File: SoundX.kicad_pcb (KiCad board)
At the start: 2 copper layers, 60.8 x 99.9 mm, 51 parts, among them CN1 EDGE_CONN, CN2 AUDIO_OUT, CN3 CONN_MIDI_IN, CN4 CONN_MIDI_OUT, U1 GAL20V8, U2 MC6850, U3 YM3526, U4 6N138, U6 YM3014, U7 LM324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

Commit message: Add clock divider for ACIA
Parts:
- added C12: 100n, Capacitor_THT:C_Disc_D7.0mm_W2.5mm_P5.00mm, F.Cu at (170.3, 90.8)
- added JP7: JMP_ACIA_CLK, Jumper:SolderJumper-3_P1.3mm_Open_RoundedPad1.0x1.5mm, B.Cu at (167.6, 98.3)
- added U5: 74HCT74, Package_DIP:DIP-14_W7.62mm_Socket_LongPads, F.Cu at (164.0, 94.6)
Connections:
- FB3 pad 1: /clock_acia -> /clk
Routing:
- net /clk: track 0.00 -> 60.3 mm, vias 0 -> 1
- net +5V: track 243.3 -> 298.8 mm, vias 4 -> 5
- net /clock_acia: track 60.6 -> 12.3 mm, vias 1 -> 0
- net /clk_quarter: track 0.00 -> 16.0 mm, vias 0 -> 2
- net Net-(U5A-D): track 0.00 -> 14.0 mm
- net Net-(U5B-D): track 0.00 -> 11.5 mm
- net /rxd_ttl: track 30.1 -> 41.0 mm, vias 1 -> 2
- net /d0: track 103.9 -> 114.4 mm, vias 3 -> 2
- net /clk_half: track 0.00 -> 10.2 mm, vias 0 -> 2
- net /ext_audio: track 138.2 -> 148.4 mm
- net /d1: track 101.4 -> 108.1 mm, vias 4 -> 2
- net /d6: track 71.4 -> 65.2 mm
- net /d7: track 76.1 -> 70.1 mm
- net /r_~{w}: track 124.6 -> 128.6 mm, vias 4 -> 3
- net /clock_ym: track 30.9 -> 32.0 mm
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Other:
- board text added: "(Set JP7 accordingly!)"
- board text added: "2M"
- board text added: "500 KHz or 2 MHz"
- board text added: "500k"
- board text added: "CC-BY-NC-SA © SukkoPera/Kinmami 2023-2024 github.com/SukkoPera/SoundX"
- board text added: "GAL20V8 or GAL22V10"
- board text removed: "500 KHz"
- board text removed: "CC-BY-NC-SA © SukkoPera/Kinmami 2023 github.com/SukkoPera/SoundX"
- board text removed: "GAL20V8 or GAL22V16"

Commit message: Final touches
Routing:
- net /d6: track 65.2 -> 64.1 mm, vias 2 -> 1
- net /d2: track 68.0 -> 69.1 mm
- net /clk_quarter: track 16.0 -> 16.9 mm
- net /d5: track 64.6 -> 64.2 mm, vias 1 -> 2
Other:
- board text added: "500 kHz or 2 MHz"
- board text removed: "500 KHz or 2 MHz"

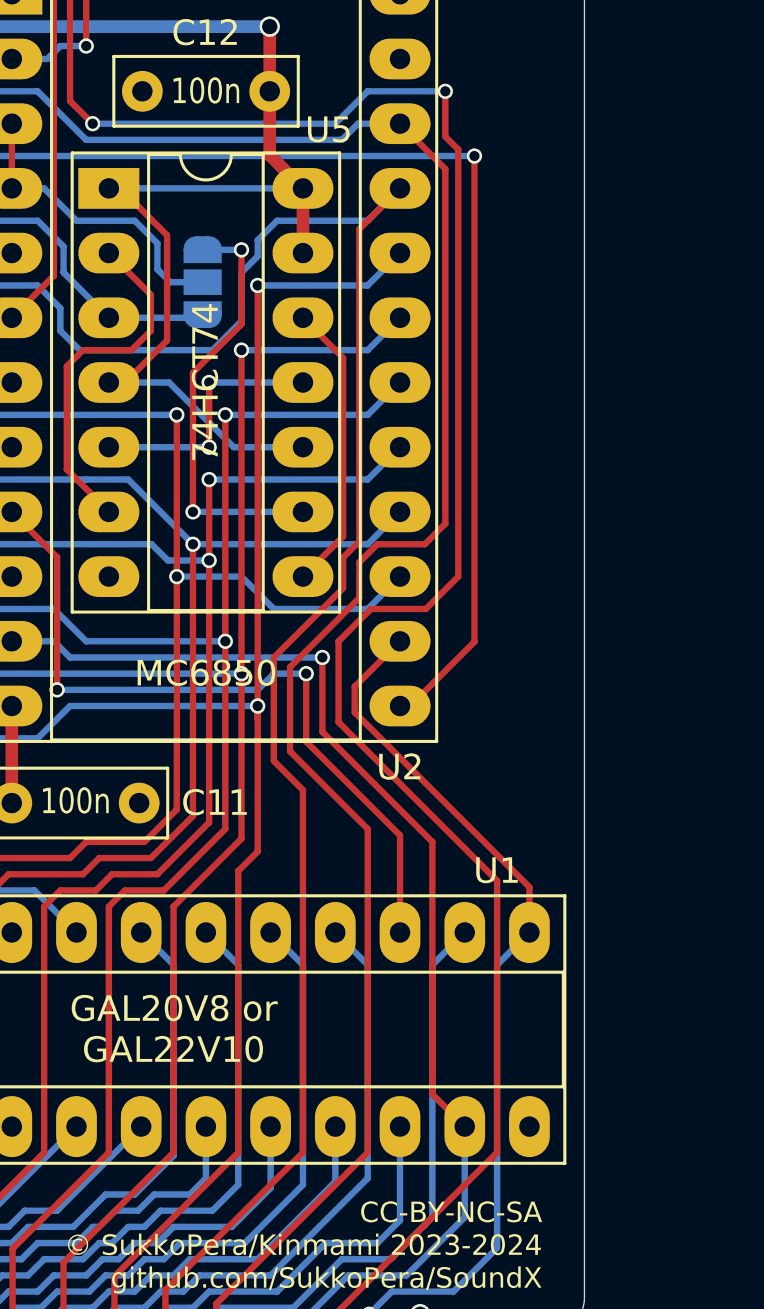
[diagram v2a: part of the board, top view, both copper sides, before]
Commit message: Add RW/A1 jumper This is inspired by some C64 interfaces
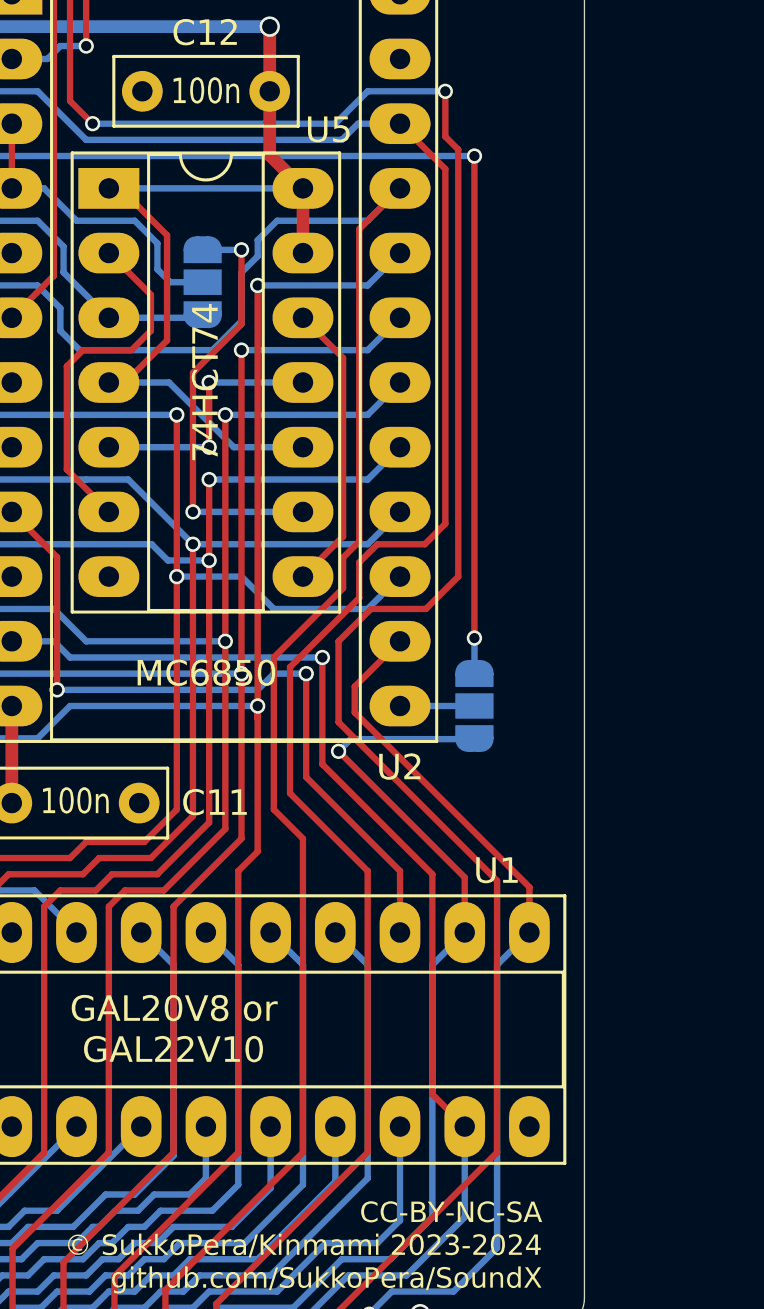
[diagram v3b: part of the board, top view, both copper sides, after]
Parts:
- added JP8: JMP_RW, Jumper:SolderJumper-3_P1.3mm_Open_RoundedPad1.0x1.5mm, B.Cu at (178.3, 114.9)
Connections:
- U2 pad 13: /r_~{w} -> Net-(JP8-C)
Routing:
- net /a1: track 28.6 -> 43.3 mm, vias 0 -> 1
- net Net-(JP8-C): track 0.00 -> 2.92 mm
- net /r_~{w}: track 128.6 -> 126.2 mm, vias 3 -> 4

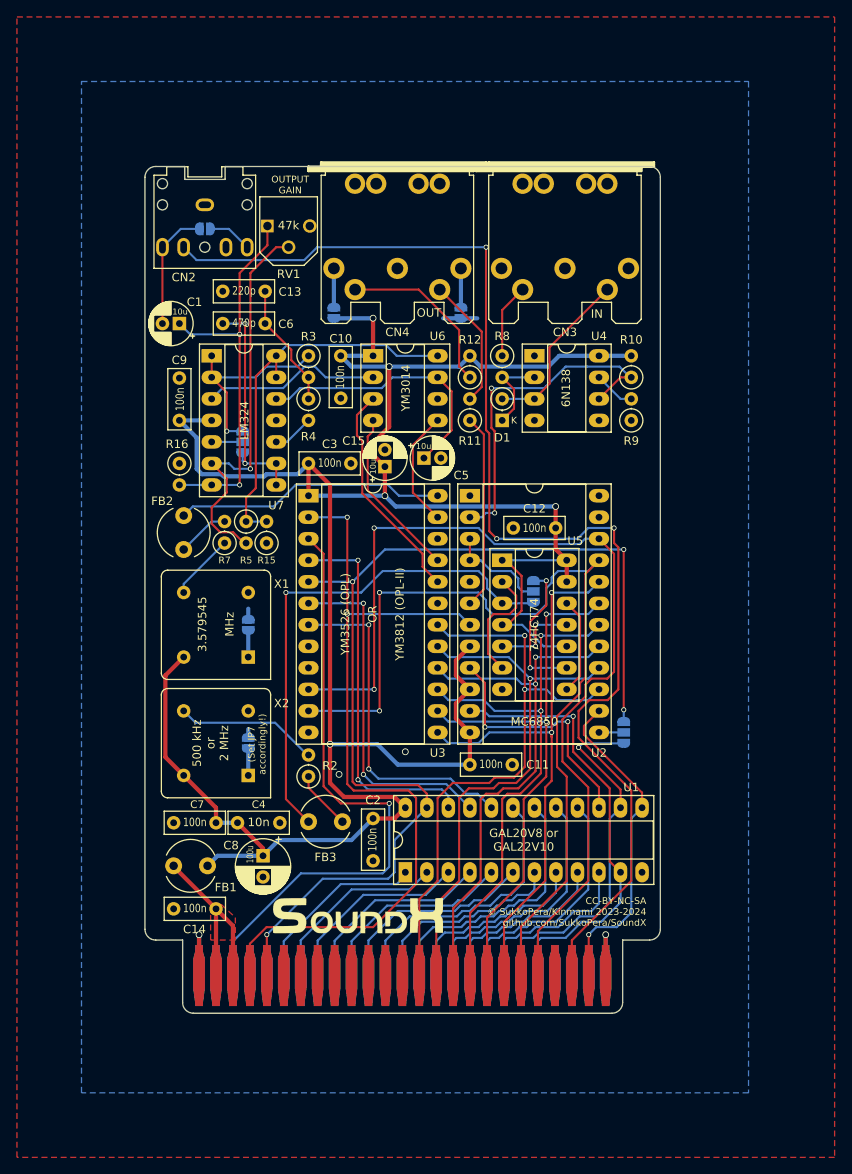
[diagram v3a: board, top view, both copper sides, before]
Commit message: 44-pin version of V2
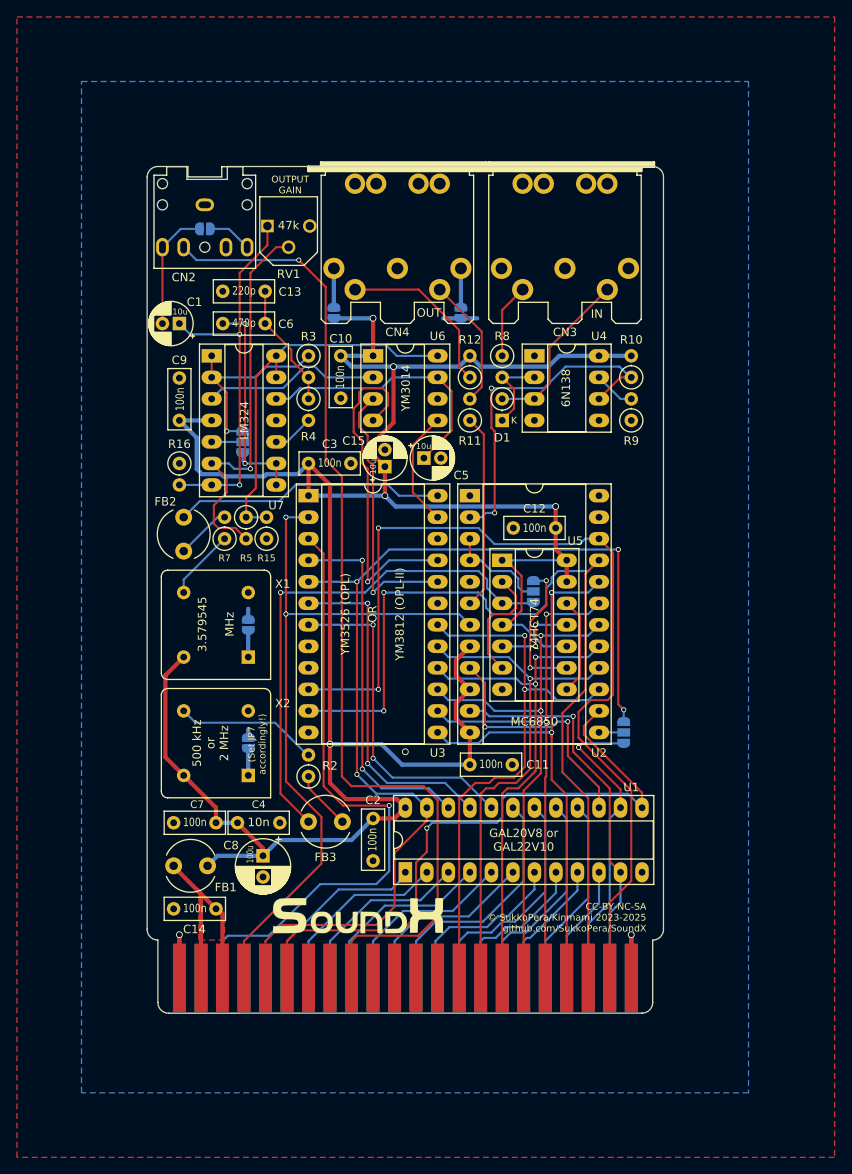
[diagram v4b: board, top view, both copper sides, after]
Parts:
- CN1: footprint SoundX:C16_Cart_Conn -> SoundX:EdgeConn-44pin
- moved CN1 29.2 mm to (123.3, 147.8)
- moved R5 0.51 mm to (133.7, 89.5)
- moved R15 0.51 mm to (136.1, 92.1)
- moved R7 0.51 mm to (131.2, 92.1)
- moved FB2 0.19 mm to (126.4, 89.5)
- turned JP8 to 90 degrees
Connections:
- CN1 pad 22: unconnected-(CN1-AEC-Pad22) -> GND
- CN1 pad 6: unconnected-(CN1-C1HI-Pad6) -> /phi2
- CN1 pad 9: unconnected-(CN1-/CS1-Pad9) -> /ext_audio
- CN1 pad Z: unconnected-(CN1-NC-PadZ) -> GND
- JP8 pad 1: /r_~{w} -> /a1
- JP8 pad 3: /a1 -> /r_~{w}
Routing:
- net /phi2: track 39.3 -> 75.7 mm
- net /ext_audio: track 148.4 -> 119.2 mm, vias 3 -> 1
- net /ser_audio: track 20.2 -> 40.4 mm, vias 0 -> 1
- net /~{irq}: track 96.7 -> 84.8 mm
- net /a2: track 21.2 -> 13.8 mm
- net /a1: track 43.3 -> 36.1 mm
- net /a0: track 52.8 -> 45.9 mm
- net /a4: track 21.7 -> 15.0 mm
- net /a3: track 29.1 -> 22.4 mm
- net /a5: track 30.7 -> 24.5 mm
- net /dac_clk: track 26.3 -> 32.4 mm, vias 0 -> 1
- net /a6: track 23.4 -> 17.7 mm
- net /a7: track 32.2 -> 27.1 mm
- net /a9: track 33.0 -> 28.9 mm
- net /a8: track 24.6 -> 20.6 mm
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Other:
- board size 60.8 x 99.9 mm -> 61 x 99.9 mm
- board text added: "A1"
- board text added: "CC-BY-NC-SA © SukkoPera/Kinmami 2023-2025 github.com/SukkoPera/SoundX"
- board text added: "R/W"
- board text removed: "CC-BY-NC-SA © SukkoPera/Kinmami 2023-2024 github.com/SukkoPera/SoundX"

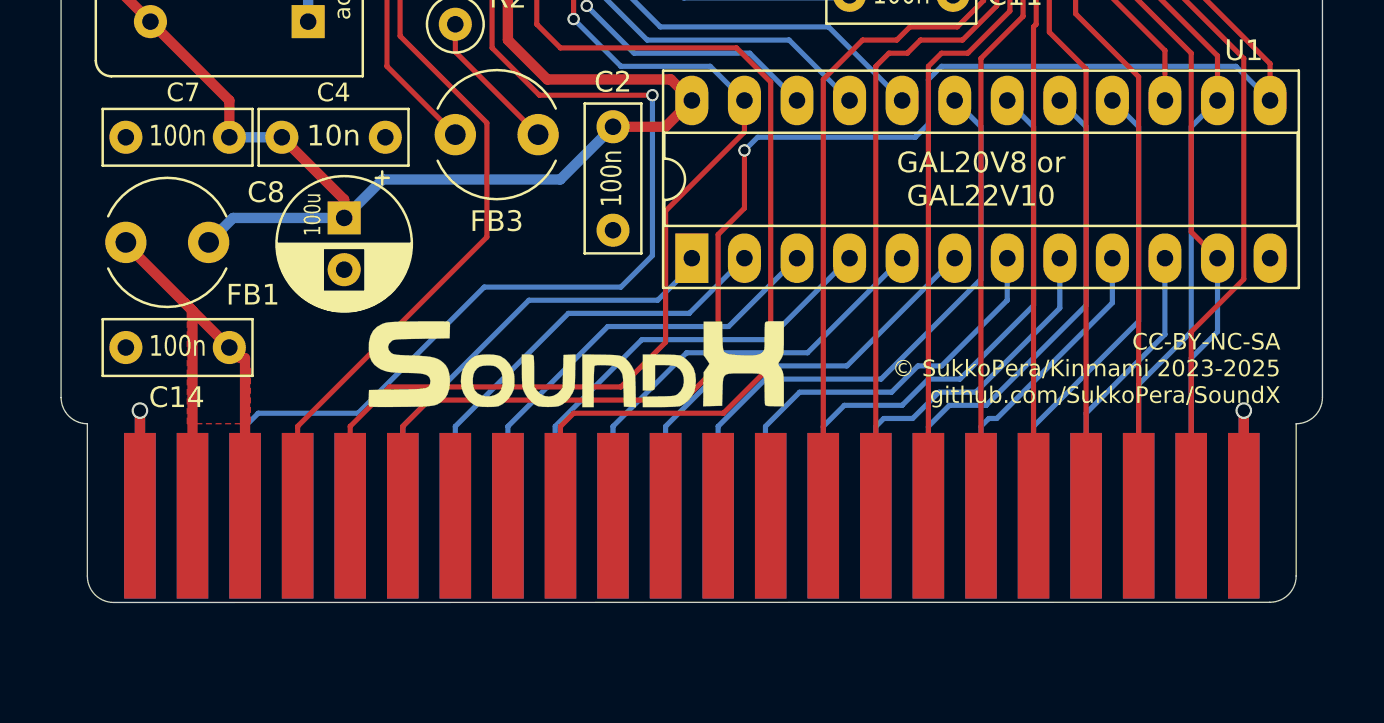
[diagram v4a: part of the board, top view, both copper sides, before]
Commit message: Better edge connector
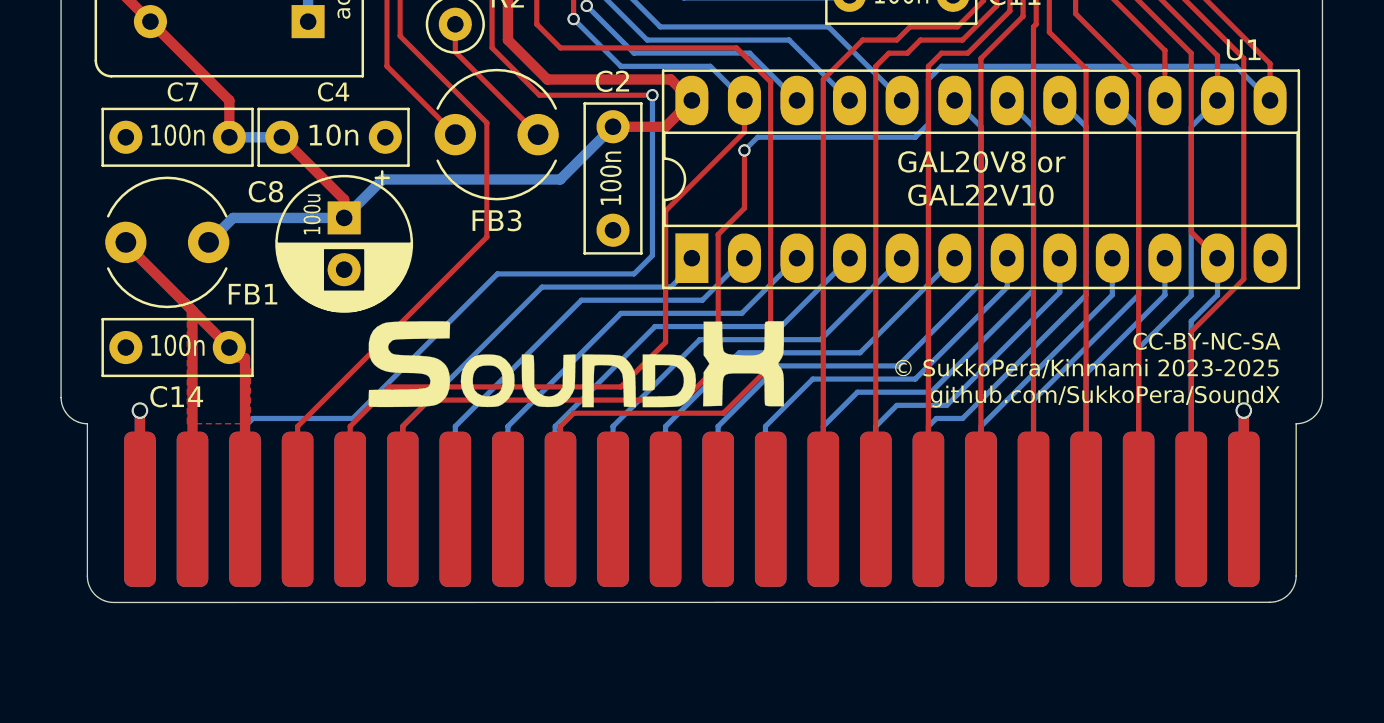
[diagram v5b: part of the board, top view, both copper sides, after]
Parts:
- moved CN1 29.2 mm to (152.5, 147.8)

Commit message: Final touches for v2_44
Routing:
- net Net-(U7B--): track 46.7 -> 44.3 mm
